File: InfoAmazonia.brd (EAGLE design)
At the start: 49 parts, among them IC1 CA3140AM Z, IC2 TL081BCDG4, IC3 AMPOP_2R, IC4 LM2662, IC5 ADAFRUIT_FONA, IC6 SHT20, IC7 MIC29302AWD, J1 BNCPTH, J2 BNCPTH, U1 ARDUINO-MEGAPRO, U2 MPL3115A2

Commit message: [INFOA-19]
- Alguns valores de componentes alterados, bom mandado pra avaliação
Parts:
- removed C16, C17: (no value), InfoAmazonia:PANASONIC_D
- added C27, C28: 47uF, InfoAmazonia:SMC_B
- IC3: value AMPOP_2R -> TL032C
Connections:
- net -5V: now also C28.-; no longer C17.-
- net GND: now also C28.+; no longer C17.+
- net N$14: now also C27.-; no longer C16.-
- net N$16: now also C27.+; no longer C16.+

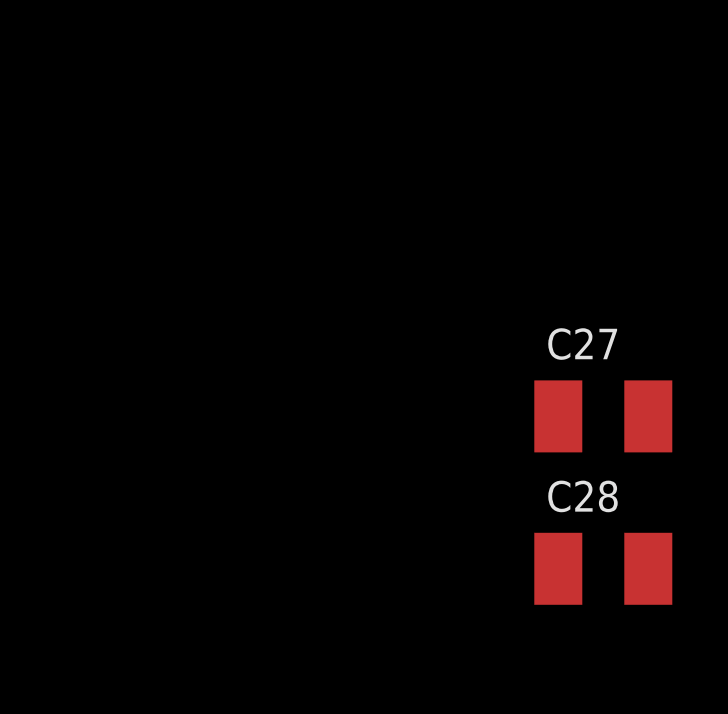
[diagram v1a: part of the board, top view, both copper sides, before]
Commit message: - SD adicionado
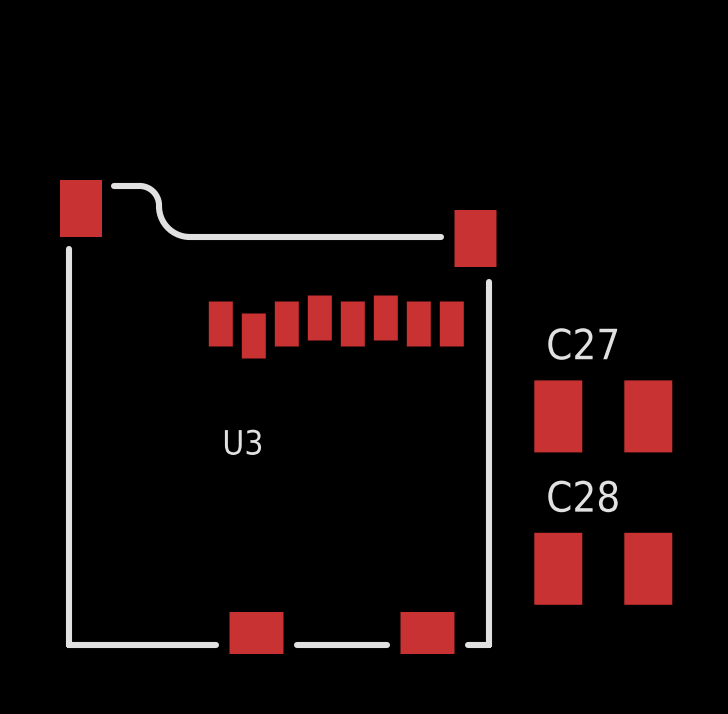
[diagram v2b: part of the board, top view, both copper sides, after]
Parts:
- added U3: USD-SOCKETNEW, InfoAmazonia:MICRO-SD-SOCKET-PP
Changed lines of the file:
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@@
 <element name="C27" library="InfoAmazonia" package="SMC_B" value="47uF" x="-105.41" y="-5.08"/>
 <element name="C28" library="InfoAmazonia" package="SMC_B" value="47uF" x="-105.41" y="-10.16"/>
+<element name="U3" library="InfoAmazonia" package="MICRO-SD-SOCKET-PP" value="USD-SOCKETNEW" x="-109.22" y="-12.7"/>
 </elements>
 <signals>

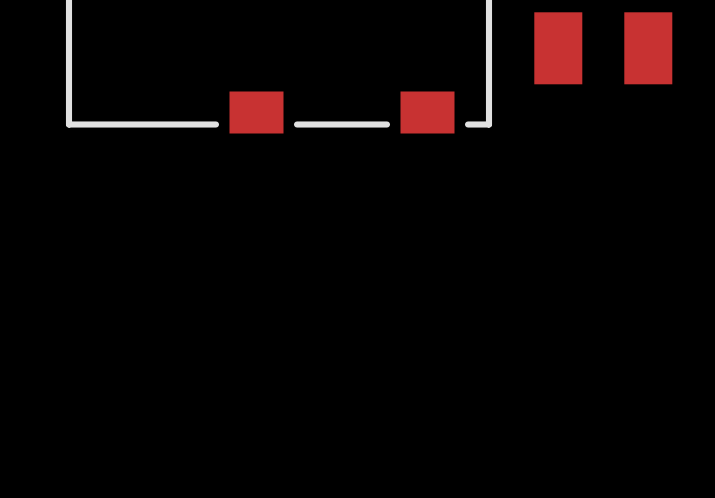
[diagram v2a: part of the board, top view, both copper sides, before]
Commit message: - SD adicionado
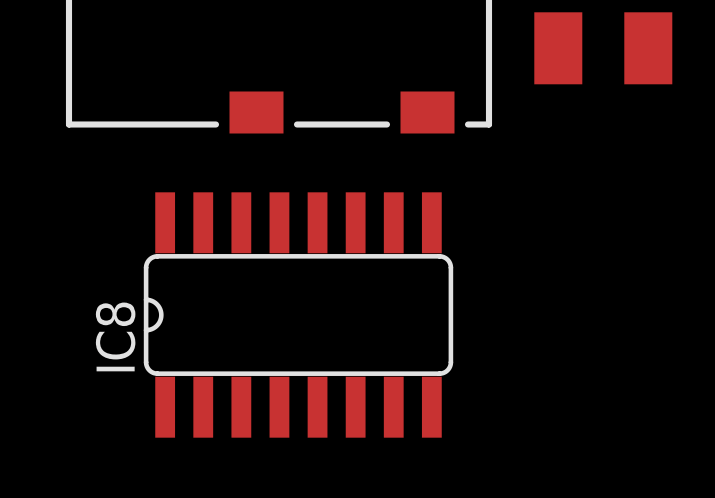
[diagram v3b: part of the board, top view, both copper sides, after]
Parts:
- added IC8: 4050D, InfoAmazonia:SO16
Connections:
- new net CS_SD: IC8.3, U1.53
- new net MISO: U1.50, U3.7
- new net MOSI: IC8.5, U1.51
- new net N$19: IC8.6, U3.5
- new net N$20: IC8.4, U3.3
- new net N$21: IC8.2, U3.2
- new net SCK: IC8.7, U1.52
- net +3V3: now also IC8.1, U3.4
- net GND: now also IC8.8, U3.6, U3.CD1, U3.CD2, U3.GND1, U3.GND3
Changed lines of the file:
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@@
 <element name="C28" library="InfoAmazonia" package="SMC_B" value="47uF" x="-105.41" y="-10.16"/>
 <element name="U3" library="InfoAmazonia" package="MICRO-SD-SOCKET-PP" value="USD-SOCKETNEW" x="-109.22" y="-12.7"/>
+<element name="IC8" library="InfoAmazonia" package="SO16" value="4050D" x="-115.57" y="-19.05"/>
 </elements>
 <signals>
@@
 <contactref element="C26" pad="-"/>
 <contactref element="C28" pad="+"/>
-<wire x1="-80.645" y1="57.09" x2="-106.91" y2="-10.16" width="0" layer="19" extent="1-1"/>
-<wire x1="-99.695" y1="62.29" x2="-80.645" y2="57.09" width="0" layer="19" extent="1-1"/>
+<contactref element="U3" pad="6"/>
+<contactref element="U3" pad="CD2"/>
+<contactref element="U3" pad="GND1"/>
+<contactref element="U3" pad="CD1"/>
+<contactref element="U3" pad="GND3"/>
+<contactref element="IC8" pad="8"/>
+<wire x1="-111.27" y1="-12.3" x2="-111.125" y2="-22.1234" width="0" layer="19" extent="1-1"/>
+<wire x1="-106.91" y1="-10.16" x2="-111.27" y2="-12.3" width="0" layer="19" extent="1-1"/>
+<wire x1="-116.97" y1="-12.3" x2="-111.27" y2="-12.3" width="0" layer="19" extent="1-1"/>
+<wire x1="-112.66" y1="-1.8" x2="-106.91" y2="-10.16" width="0" layer="19" extent="1-1"/>
+<wire x1="-109.67" y1="0.85" x2="-112.66" y2="-1.8" width="0" layer="19" extent="1-1"/>
+<wire x1="-122.82" y1="1.85" x2="-112.66" y2="-1.8" width="0" layer="19" extent="1-1"/>
+<wire x1="-99.695" y1="62.29" x2="-109.67" y2="0.85" width="0" layer="19" extent="1-1"/>
+<wire x1="-80.645" y1="57.09" x2="-99.695" y2="62.29" width="0" layer="19" extent="1-1"/>
 <wire x1="-102.02" y1="106.68" x2="-99.695" y2="62.29" width="0" layer="19" extent="1-1"/>
 <wire x1="-94.4" y1="106.68" x2="-102.02" y2="106.68" width="0" layer="19" extent="1-1"/>
@@
 <contactref element="IC6" pad="5"/>
 <contactref element="C21" pad="1"/>
-<wire x1="-41.49" y1="118.11" x2="-26.25" y2="118.11" width="0" layer="19" extent="1-1"/>
+<contactref element="U3" pad="4"/>
+<contactref element="IC8" pad="1"/>
+<wire x1="-114.86" y1="-1.8" x2="-120.015" y2="-22.1234" width="0" layer="19" extent="1-1"/>
+<wire x1="-92.29" y1="118.11" x2="-114.86" y2="-1.8" width="0" layer="19" extent="1-1"/>
+<wire x1="-49.53" y1="124.69" x2="-92.29" y2="118.11" width="0" layer="19" extent="1-1"/>
+<wire x1="-41.49" y1="118.11" x2="-49.53" y2="124.69" width="0" layer="19" extent="1-1"/>
 <wire x1="-40.57" y1="109.825" x2="-41.49" y2="118.11" width="0" layer="19" extent="1-1"/>
 <wire x1="-40.57" y1="106.075" x2="-40.57" y2="109.825" width="0" layer="19" extent="1-1"/>
-<wire x1="-49.53" y1="124.69" x2="-41.49" y2="118.11" width="0" layer="19" extent="1-1"/>
-<wire x1="-92.29" y1="118.11" x2="-49.53" y2="124.69" width="0" layer="19" extent="1-1"/>
+<wire x1="-26.25" y1="118.11" x2="-41.49" y2="118.11" width="0" layer="19" extent="1-1"/>
 <wire x1="24.13" y1="2.54" x2="-40.57" y2="106.075" width="0" layer="19" extent="1-1"/>
 </signal>
@@
 <wire x1="27.94" y1="29.21" x2="28.79" y2="25.4" width="0" layer="19" extent="1-1"/>
 </signal>
+<signal name="CS_SD">
+<contactref element="IC8" pad="3"/>
+<contactref element="U1" pad="53"/>
+<wire x1="85.09" y1="10.16" x2="-117.475" y2="-22.1234" width="0" layer="19" extent="1-1"/>
+</signal>
+<signal name="MOSI">
+<contactref element="IC8" pad="5"/>
+<contactref element="U1" pad="51"/>
+<wire x1="85.09" y1="12.7" x2="-114.935" y2="-22.1234" width="0" layer="19" extent="1-1"/>
+</signal>
+<signal name="N$19">
+<contactref element="U3" pad="5"/>
+<contactref element="IC8" pad="6"/>
+<wire x1="-113.76" y1="-2" x2="-113.665" y2="-22.1234" width="0" layer="19" extent="1-1"/>
+</signal>
+<signal name="N$20">
+<contactref element="U3" pad="3"/>
+<contactref element="IC8" pad="4"/>
+<wire x1="-115.96" y1="-2" x2="-116.205" y2="-22.1234" width="0" layer="19" extent="1-1"/>
+</signal>
+<signal name="N$21">
+<contactref element="U3" pad="2"/>
+<contactref element="IC8" pad="2"/>
+<wire x1="-117.06" y1="-2.4" x2="-118.745" y2="-22.1234" width="0" layer="19" extent="1-1"/>
+</signal>
+<signal name="MISO">
+<contactref element="U3" pad="7"/>
+<contactref element="U1" pad="50"/>
+<wire x1="82.55" y1="12.7" x2="-111.56" y2="-2" width="0" layer="19" extent="1-1"/>
+</signal>
+<signal name="SCK">
+<contactref element="IC8" pad="7"/>
+<contactref element="U1" pad="52"/>
+<wire x1="82.55" y1="10.16" x2="-112.395" y2="-22.1234" width="0" layer="19" extent="1-1"/>
+</signal>
 </signals>

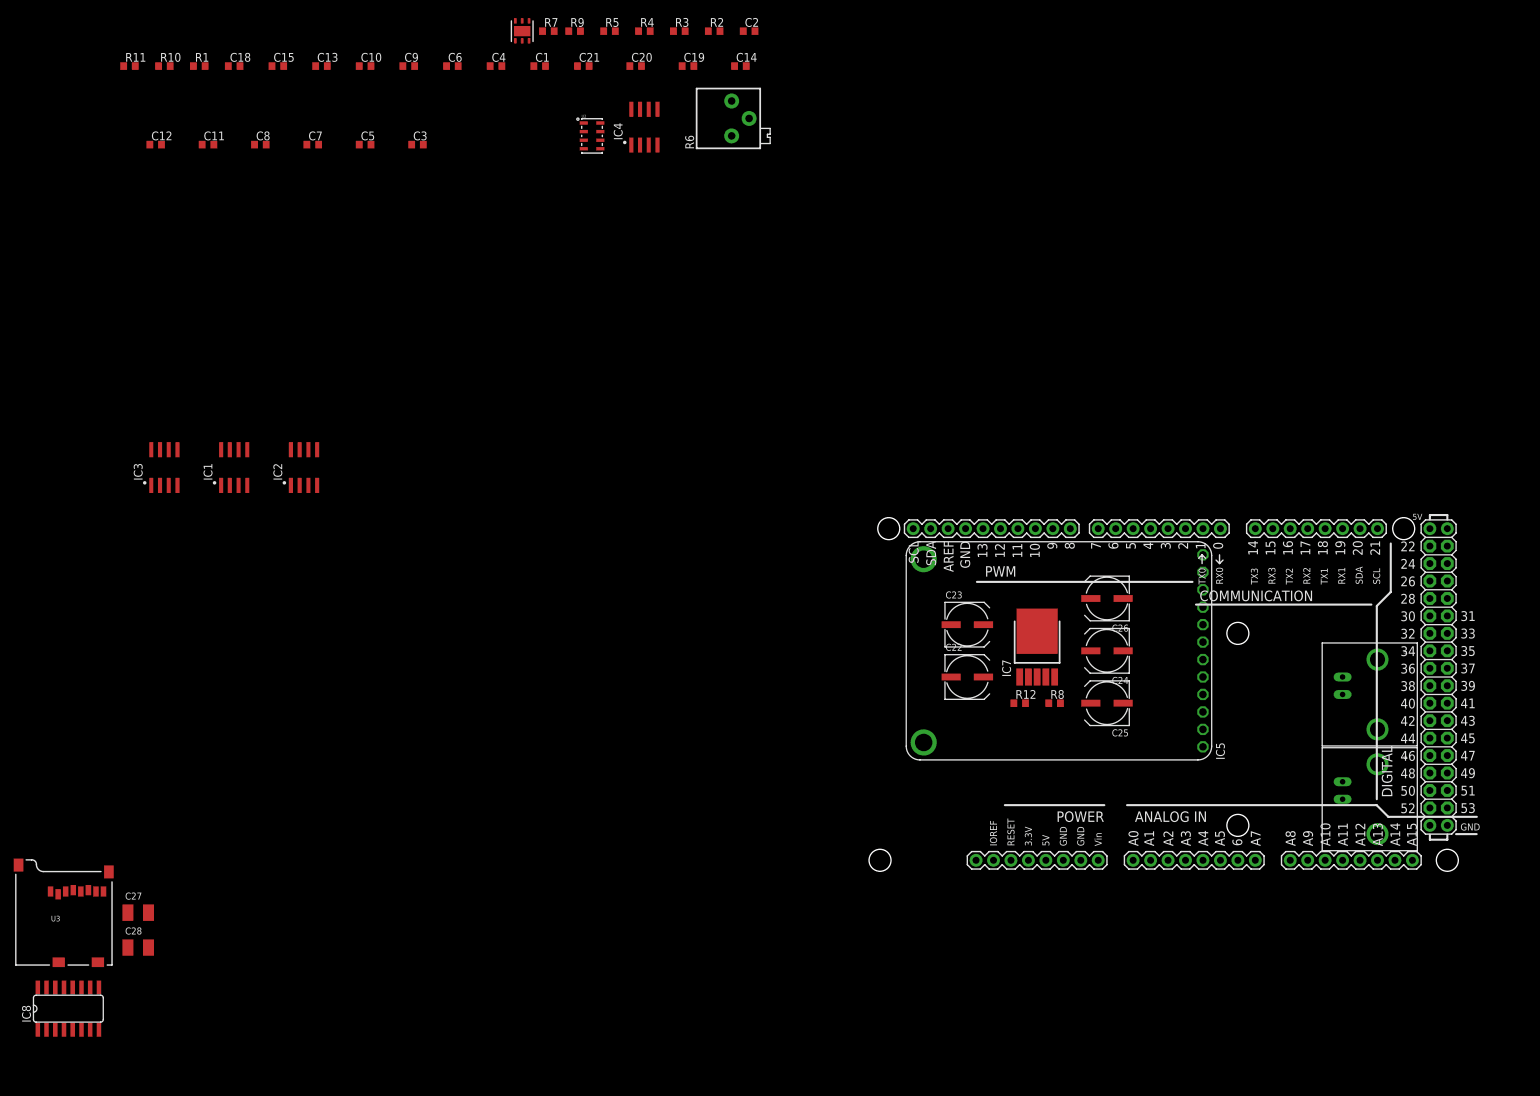
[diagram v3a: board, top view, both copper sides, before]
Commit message: - Decidido que sera utilizado o sensor do rifle pra EC
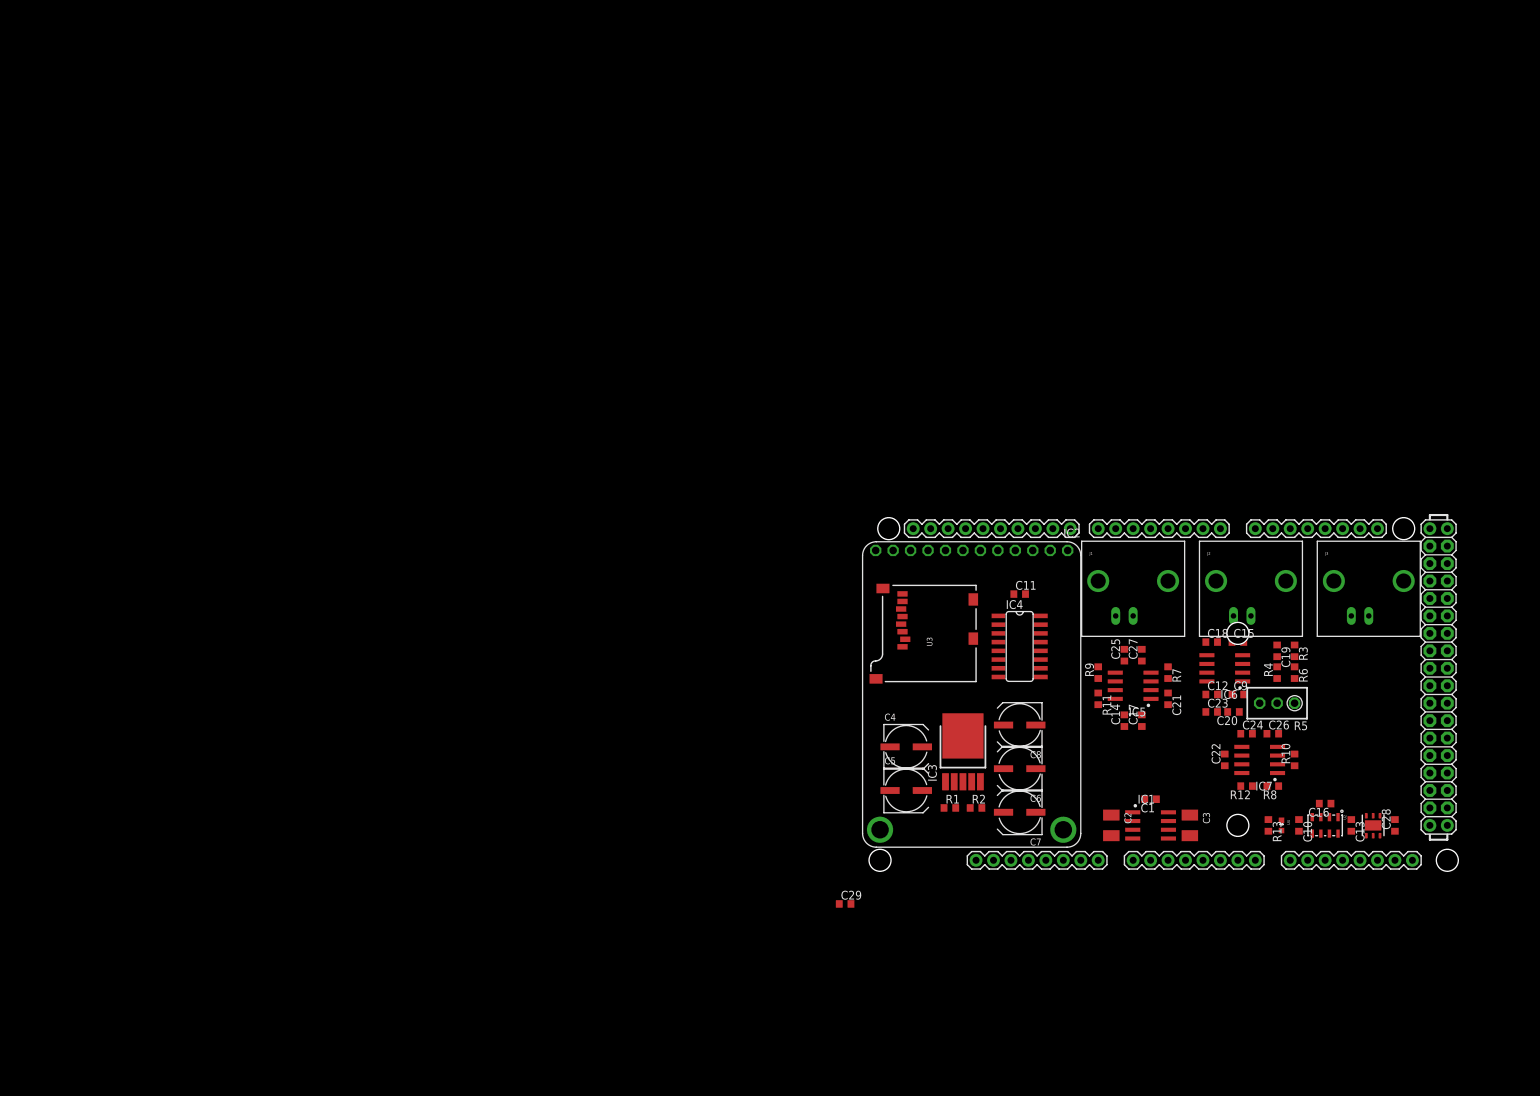
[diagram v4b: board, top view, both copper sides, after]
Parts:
- added C16: 100nF, InfoAmazonia:C0603
- added C17, C29: 10uF, InfoAmazonia:C0603
- added J3: BNCPTH, InfoAmazonia:BNC
- added R13: 2k2, InfoAmazonia:R0603
- added U4: ALS_PT19, InfoAmazonia:ALS-PT19
- C1: value 2.2nF -> 100nF
- C12: value 100nF -> 10uF
- C13, C15, C9: value 10uF -> 100nF
- C19: value 100nF -> 2.2nF
- C2: value 1uF -> 47uF; device InfoAmazonia:C0603 -> InfoAmazonia:SMC_B
- C20: value 100nF -> 1uF
- C22, C24, C25: value 220uF -> 100nF; device InfoAmazonia:UD-6,3X5,8_NICHICON -> InfoAmazonia:C0603
- C23, C26: value 220uF -> 10uF; device InfoAmazonia:UD-6,3X5,8_NICHICON -> InfoAmazonia:C0603
- C27: value 47uF -> 10uF; device InfoAmazonia:SMC_B -> InfoAmazonia:C0603
- C28: value 47uF -> 100nF; device InfoAmazonia:SMC_B -> InfoAmazonia:C0603
- C3: value 100nF -> 47uF; device InfoAmazonia:C0603 -> InfoAmazonia:SMC_B
- C4, C6: value 10uF -> 220uF; device InfoAmazonia:C0603 -> InfoAmazonia:UD-6,3X5,8_NICHICON
- C5, C7, C8: value 100nF -> 220uF; device InfoAmazonia:C0603 -> InfoAmazonia:UD-6,3X5,8_NICHICON
- IC1: value CA3140AM Z -> LM2662
- IC2: value TL081BCDG4 -> ADAFRUIT_FONA; device InfoAmazonia:SO8 -> InfoAmazonia:ADAFRUIT_FONA
- IC3: value TL032C -> MIC29302AWD; device InfoAmazonia:SO8 -> InfoAmazonia:TO252-5
- IC4: value LM2662 -> 4050D; device InfoAmazonia:SO8 -> InfoAmazonia:SO16
- IC5: value ADAFRUIT_FONA -> TL032C; device InfoAmazonia:ADAFRUIT_FONA -> InfoAmazonia:SO8
- IC6: value SHT20 -> CA3140AM Z; device InfoAmazonia:SHT2X -> InfoAmazonia:SO8
- IC7: value MIC29302AWD -> TL081BCDG4; device InfoAmazonia:TO252-5 -> InfoAmazonia:SO8
- IC8: value 4050D -> SHT20; device InfoAmazonia:SO16 -> InfoAmazonia:SHT2X
- R1: value 4M7 -> 43k
- R10, R9: value 30k -> 75k
- R11: value 75k -> 30k
- R12: value 43k -> 30k
- R2: value 2k2 -> 100k
- R3: value 30k -> 4M7
- R4: value 75k -> 1k
- R5: value 30k -> 5k; device InfoAmazonia:R0603 -> InfoAmazonia:RTRIM3296W
- R6: value 5k -> 2k2; device InfoAmazonia:RTRIM3296P -> InfoAmazonia:R0603
- R7: value 1k -> 30k
- R8: value 100k -> 30k
- moved R10 193.0 mm to (62.9, 17.1), turned to 90 degrees
- moved IC8 191.7 mm to (74.3, 7.62), turned to 180 degrees
- moved C13 186.2 mm to (71.1, 7.62), turned to 270 degrees
- moved C28 183.7 mm to (77.5, 7.62), turned to 90 degrees
- moved C10 175.1 mm to (63.5, 7.62), turned to 270 degrees
- moved C12 173.3 mm to (50.8, 26.7)
- moved R11 168.4 mm to (34.3, 26.0), turned to 270 degrees
- moved C18 165.1 mm to (50.8, 34.3)
- moved C15 162.9 mm to (54.6, 34.3)
- moved R1 153.6 mm to (12.7, 10.2)
- moved C9 151.4 mm to (54.6, 26.7)
- moved C27 150.8 mm to (40.6, 32.4), turned to 90 degrees
- moved C3 149.8 mm to (47.6, 7.62), turned to 270 degrees
- moved U2 146.4 mm to (67.3, 7.62), turned to 270 degrees
- moved IC1 143.2 mm to (41.9, 7.62), turned to 270 degrees
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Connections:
- removed net N$10: C6.2
- removed net N$11: C6.1
- removed net N$12: C5.1
- net +3V3: now also C10.1, C11.1, C13.1, C28.1, C29.1, IC4.1, IC8.5, U4.C; no longer C18.1, C19.1, C21.1, IC6.5, IC8.1
- net +5V: now also C1.1, C12.1, C14.1, C17.1, C22.1, C23.1, C4.+, C5.+, IC1.8, IC3.2, IC5.8, IC6.7, IC7.7; no longer C11.1, C13.1, C22.+, C23.+, C3.1, C4.1, C7.1, IC1.7, IC2.7, IC3.8, IC4.8, IC7.2
- net +VBAT: now also C6.+, C7.+, C8.+, IC3.4, R2.1; no longer C24.+, C25.+, C26.+, IC7.4, R8.1
- net -5V: now also C18.1, C24.1, C25.1, C26.1, C27.1, C3.-, IC1.5, IC5.4, IC6.4, IC7.4, R10.2, R9.2; no longer C10.1, C14.1, C28.-, C8.1, IC1.4, IC2.4, IC3.4, IC4.5, R11.2, R4.2
- net CS_SD: now also IC4.3; no longer IC8.3
- net FC(SD): now also IC1.1; no longer IC4.1
- net GND: now also C16.2, C17.2, C22.2, C23.2, C24.2, C25.2, C26.2, C27.2, C28.2, C29.2, C3.+, C4.-, C5.-, C6.-, C7.-, C8.-, IC1.3, IC1.6, IC3.3, IC3.6, IC4.8, IC5.5, IC8.2, IC8.7, R1.1, R13.1, R4.2; no longer C20.2, C22.-, C23.-, C24.-, C25.-, C26.-, C28.+, C3.2, C4.2, C7.2, C8.2, IC2.3, IC3.5, IC4.3, IC4.6, IC6.2, IC6.7, IC7.6, IC8.8, R12.1, R7.2
- net MOSI: now also IC4.5; no longer IC8.5
- net N$1: now also J2.S, R3.1; no longer J1.S, R1.1
- net N$13: now also IC5.3, J1.S; no longer IC3.3, J2.S
- net N$14: now also C2.-, IC1.4; no longer C27.-, IC4.4
- net N$15: now also C21.1, IC5.1, IC5.2, R7.2; no longer C12.1, IC3.1, IC3.2, R10.2
- net N$16: now also C2.+, IC1.2; no longer C27.+, IC4.2
- net N$17: now also IC5.6, R7.1; no longer IC3.6, R10.1
- net N$18: now also IC3.5, R1.2, R2.2; no longer IC7.5, R12.2, R8.2
- net N$19: now also IC4.6; no longer IC8.6
- net N$2: now also C19.1, IC6.3, R3.2; no longer C1.1, IC1.3, R1.2
- net N$20: now also IC4.4; no longer IC8.4
- net N$21: now also IC4.2; no longer IC8.2
- net N$3: now also C20.1, IC6.2, R5.2; no longer C2.1, IC1.2, R6.2
- net N$4: now also C20.2, IC6.6, R6.2, R8.2; no longer C2.2, IC1.6, R2.2, R3.2
- net N$5: now also IC7.2, R10.1, R12.1, R8.1; no longer IC2.2, R3.1, R4.1, R5.1
- net N$6: now also R4.1, R5.3; no longer R6.3, R7.1
- net N$7: now also C16.1; no longer C20.1
- net N$8: now also R5.1; no longer R2.1
- net N$9: now also R13.2, U4.E; no longer C5.2
- net OPR_SENSOR: now also IC5.7, R11.2; no longer IC3.7, R9.2
- net PH_SENSOR: now also IC7.6, R12.2; no longer IC2.6, R5.2
- net SCK: now also IC4.7; no longer IC8.7
